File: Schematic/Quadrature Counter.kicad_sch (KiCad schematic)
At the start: 8 parts, among them U26 LS7366R-S, U27 LS7366R-S, Y1 ASV-30.000MHZ-E-T

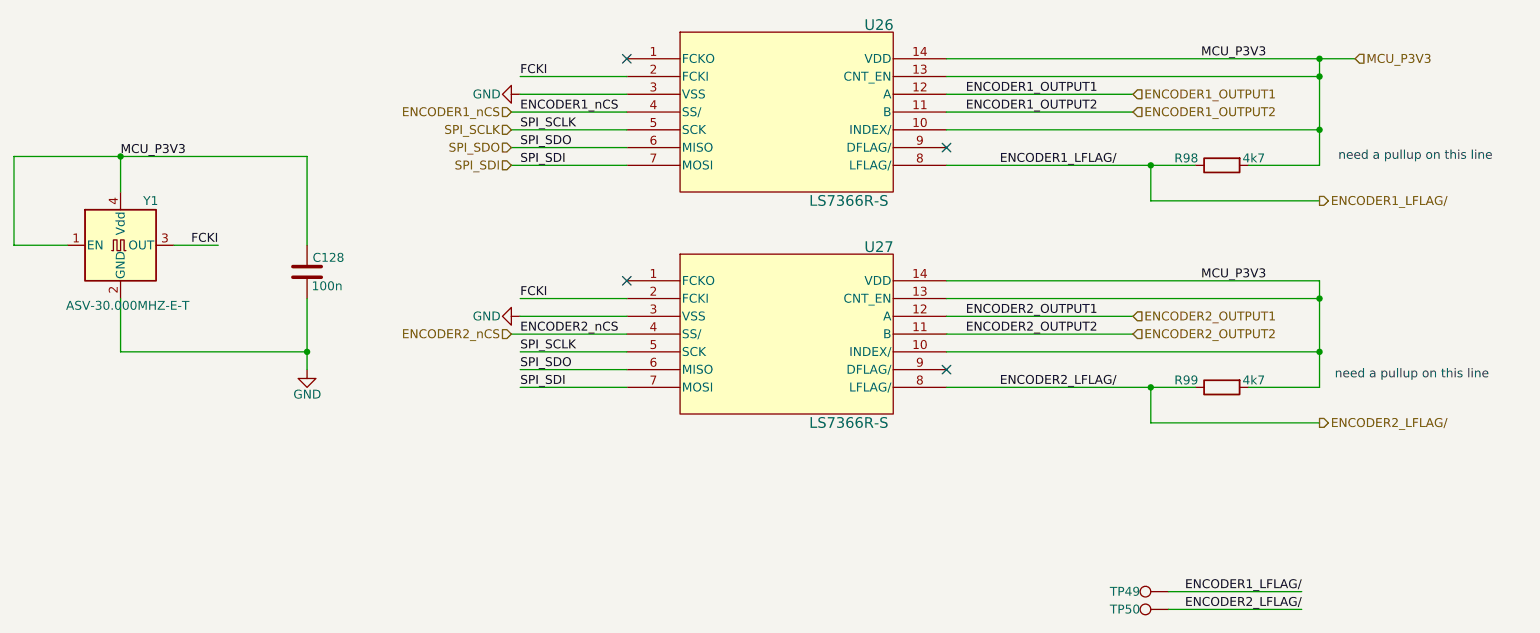
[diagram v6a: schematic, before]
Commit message: Added fuse, more footprints, and cleaned up some things
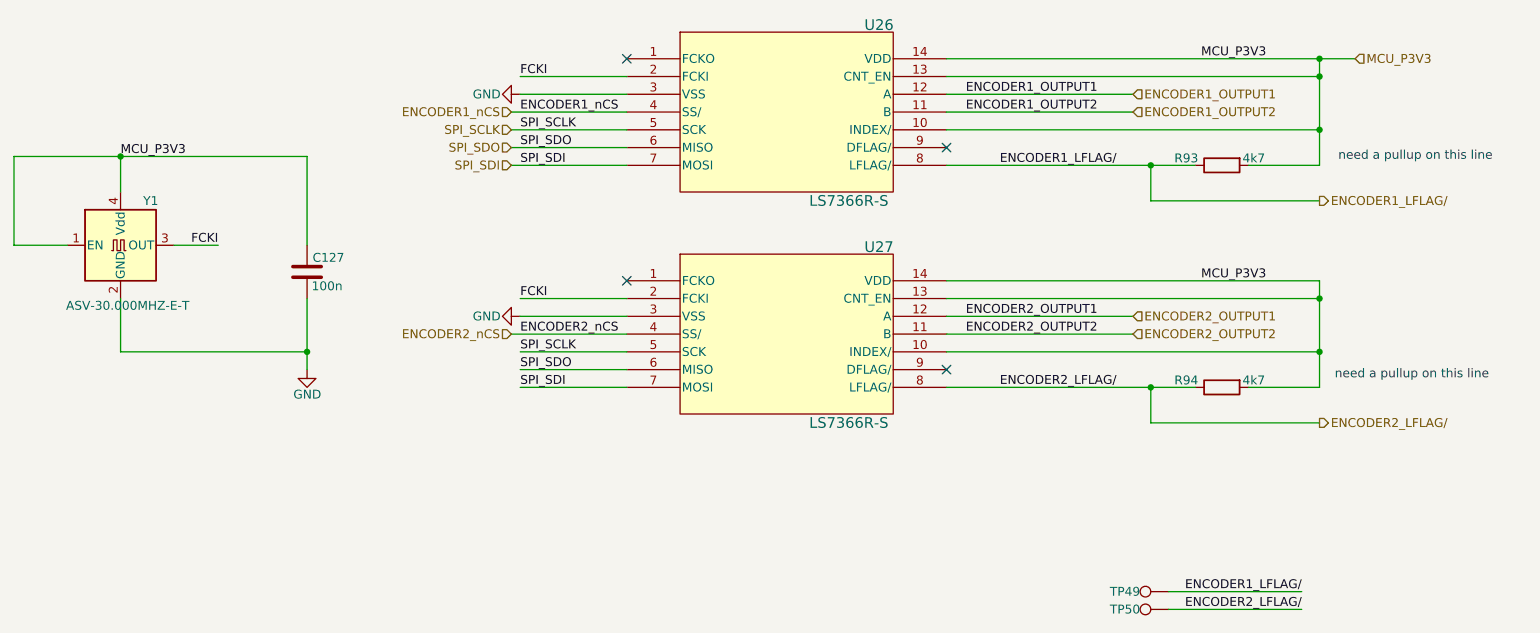
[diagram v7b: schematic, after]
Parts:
- renumbered C128 to C127, R98 to R93, R99 to R94
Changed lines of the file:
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@@
 		(on_board yes)
 		(dnp no)
-		(property "Reference" "#PWR077"
+		(property "Reference" "#PWR074"
 			(at 92.71 107.95 0)
 			(effects
@@
 			(project "STAR"
 				(path "/fc8533bc-25dd-4c20-9b4c-ffebebd6739b/f73d6367-f3ba-42df-a3ea-bd155f1c219f/12bd6774-3c71-41d8-bbdc-bae46e746955"
-					(reference "#PWR077")
+					(reference "#PWR074")
 					(unit 1)
 				)
@@
 		(on_board yes)
 		(dnp no)
-		(property "Reference" "R98"
+		(property "Reference" "R93"
 			(at 194.31 85.344 90)
 			(effects
@@
 			(project "STAR"
 				(path "/fc8533bc-25dd-4c20-9b4c-ffebebd6739b/f73d6367-f3ba-42df-a3ea-bd155f1c219f/12bd6774-3c71-41d8-bbdc-bae46e746955"
-					(reference "R98")
+					(reference "R93")
 					(unit 1)
 				)
@@
 		(on_board yes)
 		(dnp no)
-		(property "Reference" "C128"
+		(property "Reference" "C127"
 			(at 73.914 99.568 0)
 			(effects
@@
 			(project "STAR"
 				(path "/fc8533bc-25dd-4c20-9b4c-ffebebd6739b/f73d6367-f3ba-42df-a3ea-bd155f1c219f/12bd6774-3c71-41d8-bbdc-bae46e746955"
-					(reference "C128")
+					(reference "C127")
 					(unit 1)
 				)
@@
 		(on_board yes)
 		(dnp no)
-		(property "Reference" "#PWR075"
+		(property "Reference" "#PWR072"
 			(at 68.58 121.92 0)
 			(effects
@@
 			(project "STAR"
 				(path "/fc8533bc-25dd-4c20-9b4c-ffebebd6739b/f73d6367-f3ba-42df-a3ea-bd155f1c219f/12bd6774-3c71-41d8-bbdc-bae46e746955"
-					(reference "#PWR075")
+					(reference "#PWR072")
 					(unit 1)
 				)
@@
 		(on_board yes)
 		(dnp no)
-		(property "Reference" "R99"
+		(property "Reference" "R94"
 			(at 194.31 117.094 90)
 			(effects
@@
 			(project "STAR"
 				(path "/fc8533bc-25dd-4c20-9b4c-ffebebd6739b/f73d6367-f3ba-42df-a3ea-bd155f1c219f/12bd6774-3c71-41d8-bbdc-bae46e746955"
-					(reference "R99")
+					(reference "R94")
 					(unit 1)
 				)
@@
 		(on_board yes)
 		(dnp no)
-		(property "Reference" "#PWR076"
+		(property "Reference" "#PWR073"
 			(at 92.71 76.2 0)
 			(effects
@@
 			(project "STAR"
 				(path "/fc8533bc-25dd-4c20-9b4c-ffebebd6739b/f73d6367-f3ba-42df-a3ea-bd155f1c219f/12bd6774-3c71-41d8-bbdc-bae46e746955"
-					(reference "#PWR076")
+					(reference "#PWR073")
 					(unit 1)
 				)

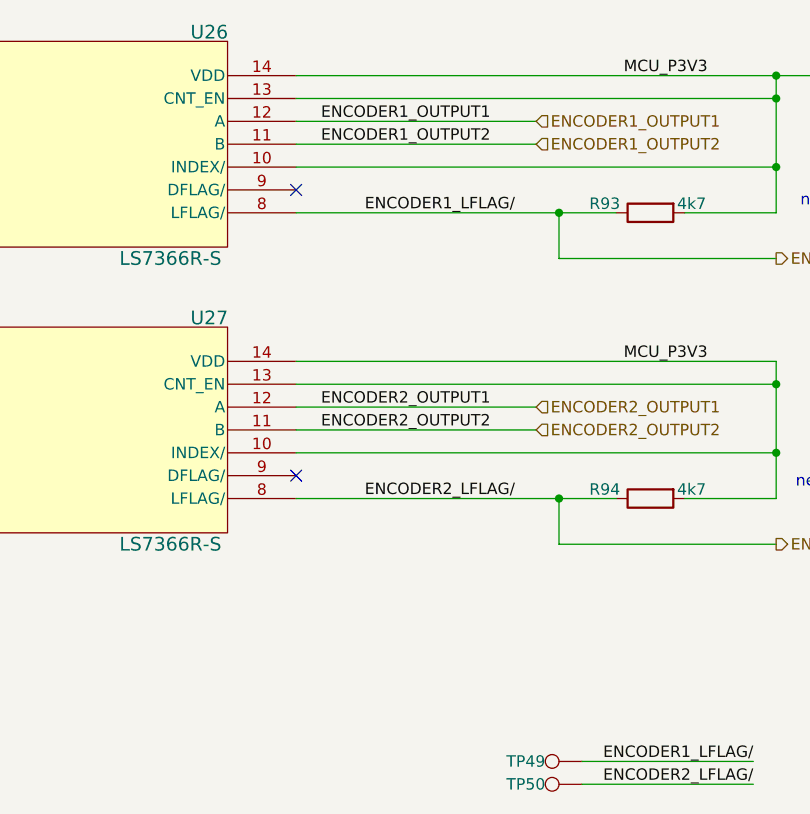
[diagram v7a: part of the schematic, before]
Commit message: added more fets and sense resistor
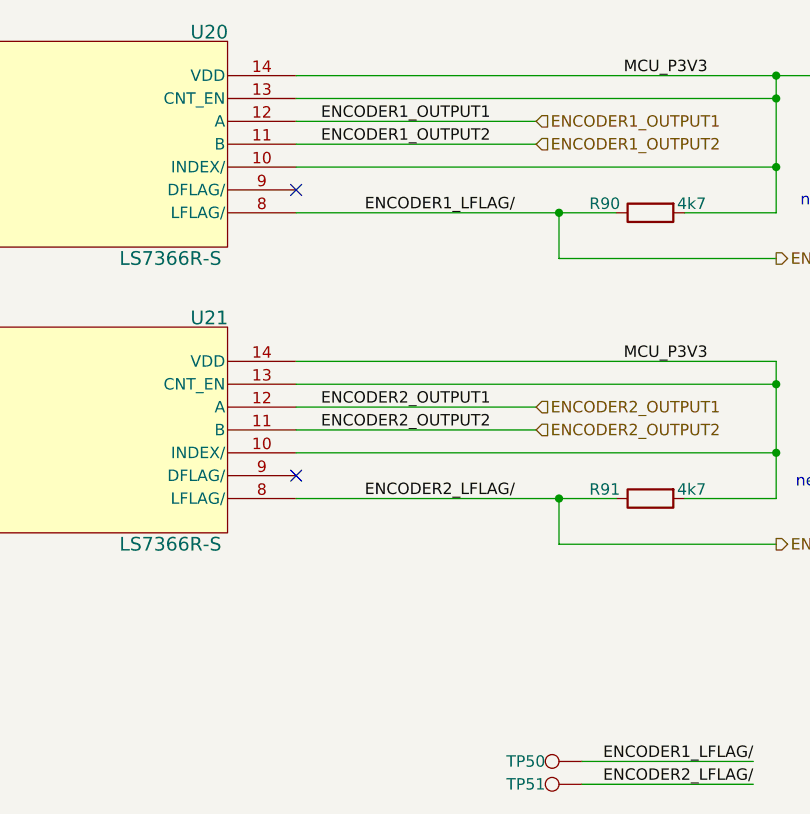
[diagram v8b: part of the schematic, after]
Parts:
- renumbered R93 to R90, R94 to R91, TP49 to TP50, TP50 to TP51, U26 to U20, U27 to U21
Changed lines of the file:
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@@
 		(on_board yes)
 		(dnp no)
-		(property "Reference" "U26"
+		(property "Reference" "U20"
 			(at 150.368 66.294 0)
 			(effects
@@
 			(project "STAR"
 				(path "/fc8533bc-25dd-4c20-9b4c-ffebebd6739b/f73d6367-f3ba-42df-a3ea-bd155f1c219f/12bd6774-3c71-41d8-bbdc-bae46e746955"
-					(reference "U26")
+					(reference "U20")
 					(unit 1)
 				)
@@
 		(on_board yes)
 		(dnp no)
-		(property "Reference" "#PWR074"
+		(property "Reference" "#PWR075"
 			(at 92.71 107.95 0)
 			(effects
@@
 			(project "STAR"
 				(path "/fc8533bc-25dd-4c20-9b4c-ffebebd6739b/f73d6367-f3ba-42df-a3ea-bd155f1c219f/12bd6774-3c71-41d8-bbdc-bae46e746955"
-					(reference "#PWR074")
+					(reference "#PWR075")
 					(unit 1)
 				)
@@
 		(on_board yes)
 		(dnp no)
-		(property "Reference" "R93"
+		(property "Reference" "R90"
 			(at 194.31 85.344 90)
 			(effects
@@
 			(project "STAR"
 				(path "/fc8533bc-25dd-4c20-9b4c-ffebebd6739b/f73d6367-f3ba-42df-a3ea-bd155f1c219f/12bd6774-3c71-41d8-bbdc-bae46e746955"
-					(reference "R93")
+					(reference "R90")
 					(unit 1)
 				)
@@
 		(on_board yes)
 		(dnp no)
-		(property "Reference" "TP49"
+		(property "Reference" "TP50"
 			(at 187.706 147.32 90)
 			(effects
@@
 			(project "STAR"
 				(path "/fc8533bc-25dd-4c20-9b4c-ffebebd6739b/f73d6367-f3ba-42df-a3ea-bd155f1c219f/12bd6774-3c71-41d8-bbdc-bae46e746955"
-					(reference "TP49")
+					(reference "TP50")
 					(unit 1)
 				)
@@
 		(on_board yes)
 		(dnp no)
-		(property "Reference" "U27"
+		(property "Reference" "U21"
 			(at 150.368 98.044 0)
 			(effects
@@
 			(project "STAR"
 				(path "/fc8533bc-25dd-4c20-9b4c-ffebebd6739b/f73d6367-f3ba-42df-a3ea-bd155f1c219f/12bd6774-3c71-41d8-bbdc-bae46e746955"
-					(reference "U27")
+					(reference "U21")
 					(unit 1)
 				)
@@
 		(on_board yes)
 		(dnp no)
-		(property "Reference" "#PWR072"
+		(property "Reference" "#PWR073"
 			(at 68.58 121.92 0)
 			(effects
@@
 			(project "STAR"
 				(path "/fc8533bc-25dd-4c20-9b4c-ffebebd6739b/f73d6367-f3ba-42df-a3ea-bd155f1c219f/12bd6774-3c71-41d8-bbdc-bae46e746955"
-					(reference "#PWR072")
+					(reference "#PWR073")
 					(unit 1)
 				)
@@
 		(on_board yes)
 		(dnp no)
-		(property "Reference" "R94"
+		(property "Reference" "R91"
 			(at 194.31 117.094 90)
 			(effects
@@
 			(project "STAR"
 				(path "/fc8533bc-25dd-4c20-9b4c-ffebebd6739b/f73d6367-f3ba-42df-a3ea-bd155f1c219f/12bd6774-3c71-41d8-bbdc-bae46e746955"
-					(reference "R94")
+					(reference "R91")
 					(unit 1)
 				)
@@
 		(on_board yes)
 		(dnp no)
-		(property "Reference" "#PWR073"
+		(property "Reference" "#PWR074"
 			(at 92.71 76.2 0)
 			(effects
@@
 			(project "STAR"
 				(path "/fc8533bc-25dd-4c20-9b4c-ffebebd6739b/f73d6367-f3ba-42df-a3ea-bd155f1c219f/12bd6774-3c71-41d8-bbdc-bae46e746955"
-					(reference "#PWR073")
+					(reference "#PWR074")
 					(unit 1)
 				)
@@
 		(on_board yes)
 		(dnp no)
-		(property "Reference" "TP50"
+		(property "Reference" "TP51"
 			(at 187.706 149.86 90)
 			(effects
@@
 			(project "STAR"
 				(path "/fc8533bc-25dd-4c20-9b4c-ffebebd6739b/f73d6367-f3ba-42df-a3ea-bd155f1c219f/12bd6774-3c71-41d8-bbdc-bae46e746955"
-					(reference "TP50")
+					(reference "TP51")
 					(unit 1)
 				)
